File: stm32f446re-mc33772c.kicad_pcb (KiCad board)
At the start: 2 copper layers, 116 parts, among them J1 Conn_01x02, J2 USB_B_Micro, J3 Conn_01x03, J4 Conn_01x06, J5 S7B-XH-A, J6 SM06B-GHS-TB, U1 STM32F446RETx, U2 MC33772CTP1AE, U3 LD1086D2M33TR, U4 AMS1117-3.3, U6 LMR51450SDRRR, U7 SN65HVD232, Y1 16MHz

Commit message: good placement
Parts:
- C10, C11, C18, C19, C48, C49, C50, C51, C52, C53, C54, C58, C59, C6, C60, C7, C8, C9, R24, R25, R26, R27, R28, R29, R30, R31, R32, R35, R36, R37: moved to B.Cu
- J3: footprint Connector_PinHeader_2.54mm:PinHeader_1x03_P2.54mm_Vertical -> Connector_PinHeader_1.00mm:PinHeader_1x03_P1.00mm_Vertical
- J4: value Conn_01x06 -> Conn_01x03; footprint Connector_PinHeader_2.54mm:PinHeader_1x06_P2.54mm_Vertical -> Connector_PinHeader_1.00mm:PinHeader_1x03_P1.00mm_Vertical
- moved C26 109.7 mm to (178.0, 54.0), turned to -90 degrees
- moved R7 106.9 mm to (176.4, 52.6), turned to 90 degrees
- moved R36 106.6 mm to (191.5, 49.0), turned to 0 degrees
- moved J3 104.8 mm to (218.9, 94.2), turned to 0 degrees
- moved D3 104.6 mm to (174.4, 53.2), turned to -90 degrees
- moved C59 104.3 mm to (191.5, 52.0), turned to 180 degrees
- moved C61 103.4 mm to (185.5, 44.0)
- moved U6 103.1 mm to (182.5, 44.0)
- moved C57 102.6 mm to (175.6, 46.7), turned to 180 degrees
- moved C56 101.6 mm to (175.6, 44.4), turned to 180 degrees
- moved C55 101.5 mm to (176.1, 42.4), turned to 180 degrees
- moved D1 100.3 mm to (159.0, 44.5)
- moved R37 99.4 mm to (192.4, 55.5), turned to 90 degrees
- moved R35 98.5 mm to (191.0, 55.5), turned to 90 degrees
- moved D2 98.1 mm to (165.6, 46.0)
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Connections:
- J3 pad 1: BAT_3.3V -> BP-C1M
- J3 pad 2: LDO_3.3V -> SWDIO
- J3 pad 3: USB_3.3V -> SWCLK
- J4 pad 1: LDO_3.3V -> BAT_3.3V
- J4 pad 2: BP-C1M -> LDO_3.3V
- J4 pad 3: SWDIO -> USB_3.3V
- U1 pad 55: SWO -> unconnected-(U1-PB3-Pad55)
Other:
- board outline added: 99 x 62.5 mm
- board text removed: "BOOT0"
- board text removed: "SWD"

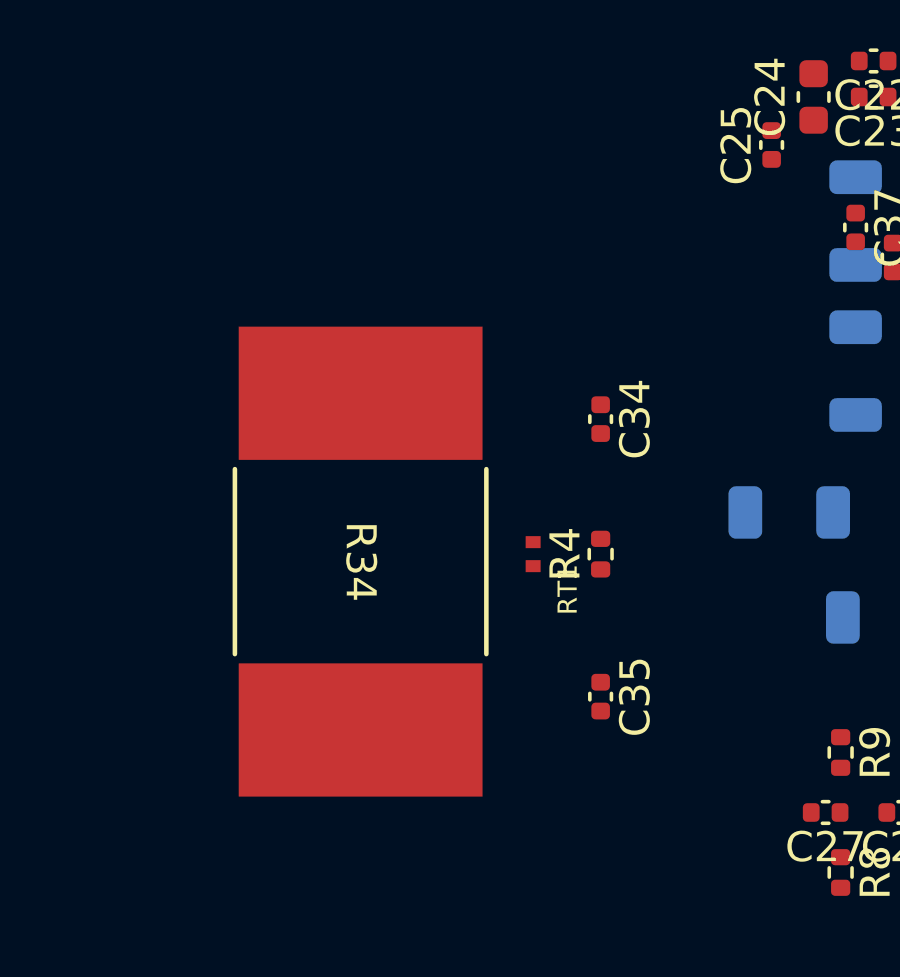
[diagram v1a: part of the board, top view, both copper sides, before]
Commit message: GND the whole in2.Cu
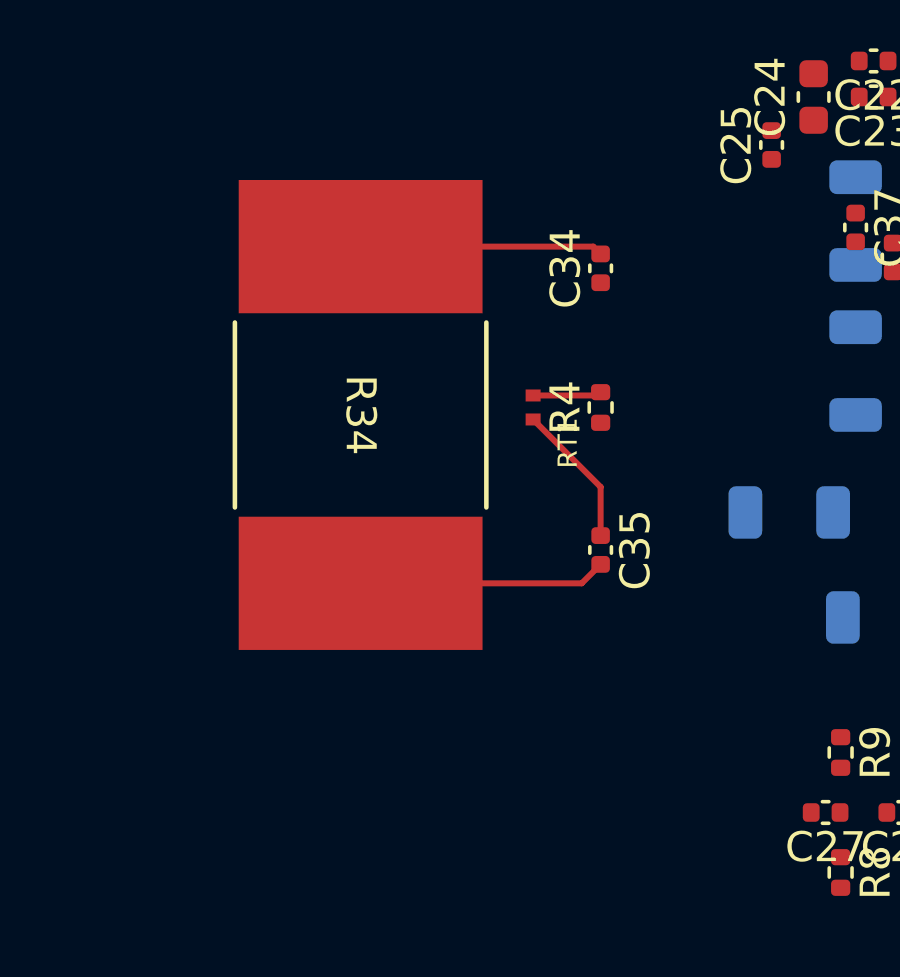
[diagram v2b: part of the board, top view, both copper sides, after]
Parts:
- moved C34 5.03 mm to (145.5, 66.1), turned to 90 degrees
- moved C35 4.89 mm to (145.5, 75.5)
- moved R34 4.89 mm to (137.5, 71.0)
- moved R4 4.89 mm to (145.5, 70.8)
- moved RT1 4.89 mm to (143.2, 70.8)
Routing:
- net BP-C1M: track 0.00 -> 12.9 mm
- net Pack-: track 0.00 -> 8.26 mm
- net Net-(R33-Pad2): track 0.00 -> 2.30 mm
- added copper zone on In2.Cu, net GND
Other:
- copper layers 2 -> 4
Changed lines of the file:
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@@
 	(layers
 		(0 "F.Cu" mixed)
+		(4 "In1.Cu" signal)
+		(6 "In2.Cu" signal)
 		(2 "B.Cu" signal)
 		(9 "F.Adhes" user "F.Adhesive")
@@
 	)
 	(setup
+		(stackup
+			(layer "F.SilkS"
+				(type "Top Silk Screen")
+			)
+			(layer "F.Paste"
+				(type "Top Solder Paste")
+			)
+			(layer "F.Mask"
+				(type "Top Solder Mask")
+				(thickness 0.01)
+			)
+			(layer "F.Cu"
+				(type "copper")
+				(thickness 0.035)
+			)
+			(layer "dielectric 1"
+				(type "prepreg")
+				(thickness 0.1)
+				(material "FR4")
+				(epsilon_r 4.5)
+				(loss_tangent 0.02)
+			)
+			(layer "In1.Cu"
+				(type "copper")
+				(thickness 0.035)
+			)
+			(layer "dielectric 2"
+				(type "core")
+				(thickness 1.24)
+				(material "FR4")
+				(epsilon_r 4.5)
+				(loss_tangent 0.02)
+			)
+			(layer "In2.Cu"
+				(type "copper")
+				(thickness 0.035)
+			)
+			(layer "dielectric 3"
+				(type "prepreg")
+				(thickness 0.1)
+				(material "FR4")
+				(epsilon_r 4.5)
+				(loss_tangent 0.02)
+			)
+			(layer "B.Cu"
+				(type "copper")
+				(thickness 0.035)
+			)
+			(layer "B.Mask"
+				(type "Bottom Solder Mask")
+				(thickness 0.01)
+			)
+			(layer "B.Paste"
+				(type "Bottom Solder Paste")
+			)
+			(layer "B.SilkS"
+				(type "Bottom Silk Screen")
+			)
+			(copper_finish "None")
+			(dielectric_constraints no)
+		)
 		(pad_to_mask_clearance 0)
 		(allow_soldermask_bridges_in_footprints no)
@@
 		(capping no)
 		(filling no)
+		(zone_defaults)
 		(pcbplotparams
 			(layerselection 0x00000000_00000000_55555555_5755f5ff)
@@
 	(footprint "Resistor_SMD:R_0402_1005Metric"
 		(layer "F.Cu")
-		(at 145.5 75.6382 90)
+		(at 145.5 70.75 90)
 		(descr "Resistor SMD 0402 (1005 Metric), square (rectangular) end terminal, IPC-7351 nominal, (Body size source: IPC-SM-782 page 72, https://www.pcb-3d.com/wordpress/wp-content/uploads/ipc-sm-782a_amendment_1_and_2.pdf)")
 		(tags "resistor")
@@
 	(footprint "Capacitor_SMD:C_0402_1005Metric"
 		(layer "F.Cu")
-		(at 145.5 71.1382 -90)
+		(at 145.5 66.1118 90)
 		(descr "Capacitor SMD 0402 (1005 Metric), square (rectangular) end terminal, IPC-7351 nominal, (Body size source: IPC-SM-782 page 76, https://www.pcb-3d.com/wordpress/wp-content/uploads/ipc-sm-782a_amendment_1_and_2.pdf)")
 		(tags "capacitor")
@@
 		(duplicate_pad_numbers_are_jumpers no)
 		(fp_line
-			(start -0.107836 0.36)
-			(end 0.107836 0.36)
+			(start -0.107836 -0.36)
+			(end 0.107836 -0.36)
 			(stroke
 				(width 0.12)
@@
 		)
 		(fp_line
-			(start -0.107836 -0.36)
-			(end 0.107836 -0.36)
+			(start -0.107836 0.36)
+			(end 0.107836 0.36)
 			(stroke
 				(width 0.12)
@@
 		)
 		(pad "1" smd roundrect
-			(at -0.48 0 270)
+			(at -0.48 0 90)
 			(size 0.56 0.62)
 			(layers "F.Cu" "F.Mask" "F.Paste")
@@
 		)
 		(pad "2" smd roundrect
-			(at 0.48 0 270)
+			(at 0.48 0 90)
 			(size 0.56 0.62)
 			(layers "F.Cu" "F.Mask" "F.Paste")
@@
 	(footprint "MyFootLib:WSLP5931L1000FEA"
 		(layer "F.Cu")
-		(at 137.5 75.8882 -90)
+		(at 137.5 71 -90)
 		(tags "WSLP5931L1000FEA ")
 		(property "Reference" "R34"
@@
 			(polygon
 				(pts
-					(xy 141.5132 72.548099) (xy 141.5132 79.228301) (xy 133.4868 79.228301) (xy 133.4868 72.548099)
+					(xy 141.5132 67.659899) (xy 141.5132 74.340101) (xy 133.4868 74.340101) (xy 133.4868 67.659899)
 				)
 			)
@@
 	(footprint "Capacitor_SMD:C_0402_1005Metric"
 		(layer "F.Cu")
-		(at 145.5 80.3882 -90)
+		(at 145.5 75.5 -90)
 		(descr "Capacitor SMD 0402 (1005 Metric), square (rectangular) end terminal, IPC-7351 nominal, (Body size source: IPC-SM-782 page 76, https://www.pcb-3d.com/wordpress/wp-content/uploads/ipc-sm-782a_amendment_1_and_2.pdf)")
 		(tags "capacitor")
@@
 	(footprint "MyFootLib:THERM_NTCG104BH103HT1"
 		(layer "F.Cu")
-		(at 143.25 75.6382 -90)
+		(at 143.25 70.75 -90)
 		(property "Reference" "RT1"
 			(at 1.182 -1.1564 90)
@@
 		(layer "Edge.Cuts")
 	)
-	(gr_text_box "PACK+"
-		(start 123.625 102.313)
-		(end 133.375 97.5)
+	(gr_text_box "GND"
+		(start 179 94.0935)
+		(end 185.5 98.9065)
 		(margins 1.0025 1.0025 1.0025 1.0025)
 		(layer "F.Cu")
@@
 		(knockout no)
 	)
-	(gr_text_box "BAT+"
-		(start 124 53)
-		(end 132.5 48.187)
-		(margins 1.0025 1.0025 1.0025 1.0025)
+	(segment
+		(start 145.5 73.4)
+		(end 143.25 71.15)
+		(width 0.2)
 		(layer "F.Cu")
-		(effects
-			(font
-				(size 1.5 1.5)
-				(thickness 0.3)
-				(bold yes)
-			)
-			(justify left top)
-		)
-		(border yes)
-		(stroke
-			(width 0.2)
-			(type solid)
-		)
-		(knockout no)
+		(net "BP-C1M")
 	)
-	(gr_text_box "PACK-"
-		(start 132.5 94.2012)
-		(end 142.25 89.3882)
-		(margins 1.0025 1.0025 1.0025 1.0025)
+	(segment
+		(start 145.5 75.02)
+		(end 145.5 73.4)
+		(width 0.2)
 		(layer "F.Cu")
-		(effects
-			(font
-				(size 1.5 1.5)
-				(thickness 0.3)
-				(bold yes)
-			)
-			(justify left top)
-		)
-		(border yes)
-		(stroke
-			(width 0.2)
-			(type solid)
-		)
-		(knockout no)
+		(net "BP-C1M")
 	)
-	(gr_text_box "BAT-"
-		(start 133.75 63.5447)
-		(end 141.25 58.7317)
-		(margins 1.0025 1.0025 1.0025 1.0025)
+	(segment
+		(start 145.2564 65.3882)
+		(end 145.5 65.6318)
+		(width 0.2)
 		(layer "F.Cu")
-		(effects
-			(font
-				(size 1.5 1.5)
-				(thickness 0.3)
-				(bold yes)
-			)
-			(justify left top)
-		)
-		(border yes)
-		(stroke
-			(width 0.2)
-			(type solid)
-		)
-		(knockout no)
+		(net "BP-C1M")
 	)
-	(gr_text_box "GND"
-		(start 179 94.0935)
-		(end 185.5 98.9065)
-		(margins 1.0025 1.0025 1.0025 1.0025)
+	(segment
+		(start 137.5 65.3882)
+		(end 145.2564 65.3882)
+		(width 0.2)
 		(layer "F.Cu")
-		(effects
-			(font
-				(size 1.5 1.5)
-				(thickness 0.3)
-				(bold yes)
-			)
-			(justify left top)
+		(net "BP-C1M")
+	)
+	(segment
+		(start 145.39 70.35)
+		(end 145.5 70.24)
+		(width 0.2)
+		(layer "F.Cu")
+		(net "Net-(R33-Pad2)")
+	)
+	(segment
+		(start 143.25 70.35)
+		(end 145.39 70.35)
+		(width 0.2)
+		(layer "F.Cu")
+		(net "Net-(R33-Pad2)")
+	)
+	(segment
+		(start 137.5 76.6118)
+		(end 144.8682 76.6118)
+		(width 0.2)
+		(layer "F.Cu")
+		(net "Pack-")
+	)
+	(segment
+		(start 144.8682 76.6118)
+		(end 145.5 75.98)
+		(width 0.2)
+		(layer "F.Cu")
+		(net "Pack-")
+	)
+	(zone
+		(net "GND")
+		(layer "In2.Cu")
+		(hatch edge 0.5)
+		(connect_pads
+			(clearance 0.5)
 		)
-		(border yes)
-		(stroke
-			(width 0.2)
-			(type solid)
+		(min_thickness 0.25)
+		(fill yes
+			(thermal_gap 0.5)
+			(thermal_bridge_width 0.5)
+			(island_removal_mode 0)
+		)
+		(polygon
+			(pts
+				(xy 121.5 40.5) (xy 121.5 103) (xy 220.5 103) (xy 220.5 40.5)
+			)
 		)
-		(knockout no)
 	)
 	(embedded_fonts no)

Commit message: start routing
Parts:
- turned R20 to -90 degrees
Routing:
- net Pack_24V: track 0.00 -> 75.5 mm
- net BP-C1M: track 12.9 -> 69.8 mm, vias 0 -> 19
- net Pack-: track 8.26 -> 24.1 mm
- net BP-C5P: track 0.00 -> 8.03 mm, vias 0 -> 1
- net BP-C2P: track 0.00 -> 7.92 mm, vias 0 -> 1
- net BP-C6P: track 0.00 -> 7.91 mm, vias 0 -> 1
- net BP-C4P: track 0.00 -> 7.91 mm, vias 0 -> 1
- net BP-C3P: track 0.00 -> 7.81 mm, vias 0 -> 1
- net BP-C1P: track 0.00 -> 7.80 mm, vias 0 -> 1
- net Net-(C33-Pad1): track 0.00 -> 2.98 mm
- net Net-(C32-Pad1): track 0.00 -> 2.98 mm
- net Net-(C31-Pad1): track 0.00 -> 2.98 mm
- net Net-(C30-Pad1): track 0.00 -> 2.98 mm
- net Net-(C29-Pad1): track 0.00 -> 2.98 mm
- net Net-(C28-Pad1): track 0.00 -> 2.98 mm
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- added copper zone on F.Cu, net BP-C1M
- added copper zone on F.Cu, net Pack-
- added copper zone on F.Cu, net Pack_24V
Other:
- board size 99 x 62.5 mm -> 105.7 x 62.5 mm
- board text added: "B+"
- board text added: "B-"
- board text added: "P+"
- board text added: "P-"

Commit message: freerouting weird wiring
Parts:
- moved D4 2.70 mm to (178.2, 96.0)
- moved C64 2.08 mm to (213.6, 86.6)
- moved C63 2.08 mm to (212.2, 86.4)
- moved C4 1.83 mm to (199.2, 50.4), turned to 90 degrees
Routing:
- net BP-C1M: track 69.8 -> 243.5 mm, vias 19 -> 49
- net LDO_3.3V: track 0.00 -> 144.7 mm, vias 0 -> 2
- net Buck_5V: track 0.00 -> 71.9 mm, vias 0 -> 2
- net BP-C6P: track 7.91 -> 79.5 mm, vias 1 -> 2
- net Pack-: track 24.1 -> 73.1 mm, vias 0 -> 2
- net D+: track 0.00 -> 46.8 mm, vias 0 -> 2
- net D-: track 0.00 -> 41.3 mm, vias 0 -> 2
- net VBAT_PROT_24V: track 0.00 -> 35.6 mm
- net SWDIO: track 0.00 -> 35.5 mm, vias 0 -> 1
- net AFE_VCOM: track 0.00 -> 34.7 mm, vias 0 -> 2
- net SPI1_SCK: track 0.00 -> 33.1 mm, vias 0 -> 2
- net SWCLK: track 0.00 -> 31.7 mm
- net SPI1_MOSI: track 0.00 -> 31.1 mm, vias 0 -> 2
- net SPI1_NSS: track 0.00 -> 30.4 mm, vias 0 -> 2
- net Net-(J1-Pin_2): track 0.00 -> 28.0 mm
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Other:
- board text added: "BOOT0"

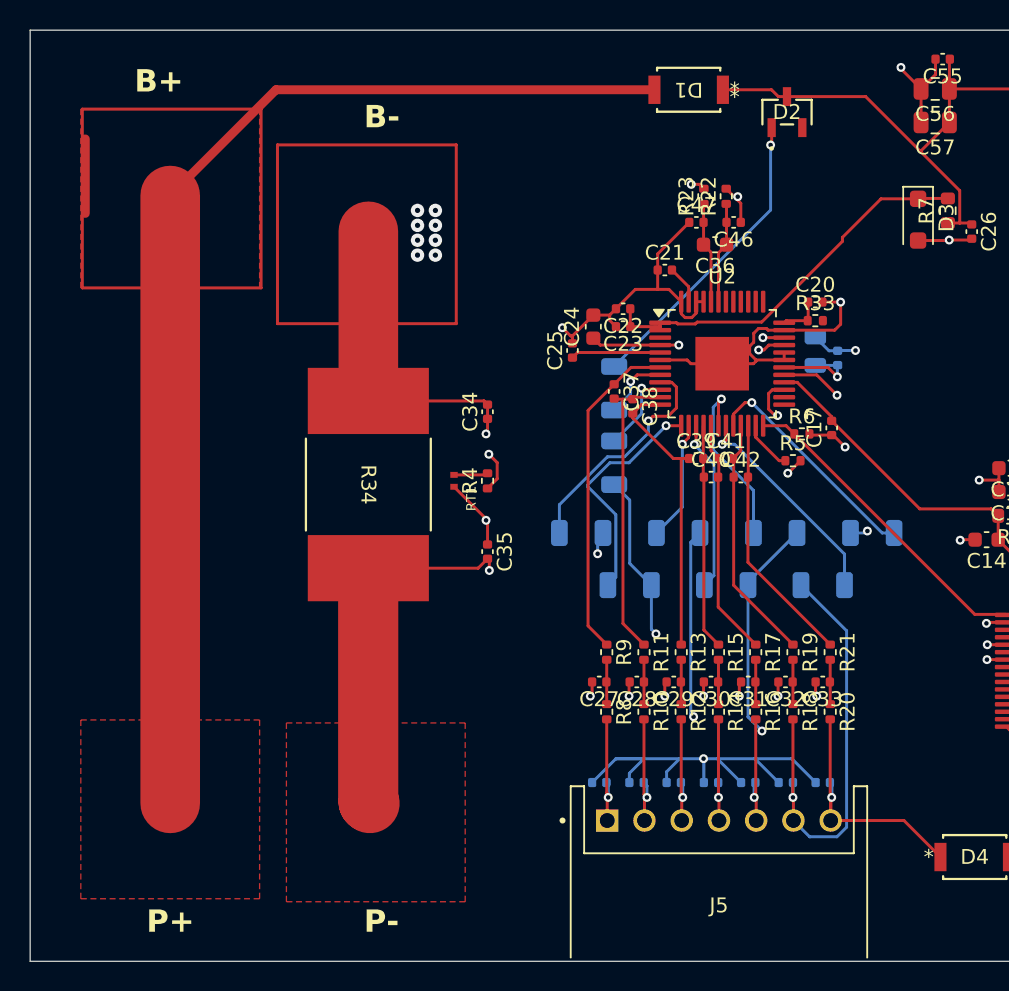
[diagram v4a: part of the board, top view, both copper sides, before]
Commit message: add pad for B and P
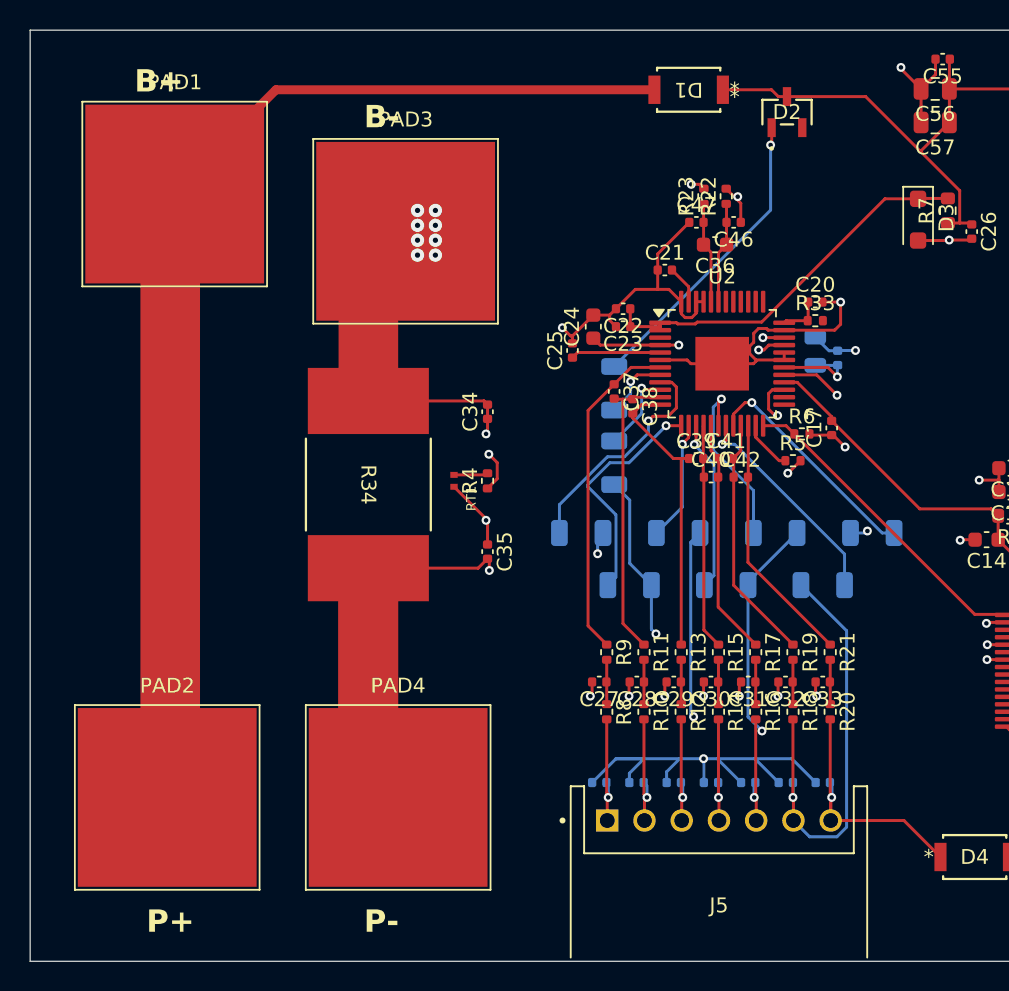
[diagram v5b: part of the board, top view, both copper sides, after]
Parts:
- added PAD1: pad, MyFootLib:INPUT_PAD, F.Cu at (124.5, 51.5)
- added PAD2: pad, MyFootLib:INPUT_PAD, F.Cu at (124.0, 92.0)
- added PAD3: pad, MyFootLib:INPUT_PAD, F.Cu at (140.0, 54.0)
- added PAD4: pad, MyFootLib:INPUT_PAD, F.Cu at (139.5, 92.0)
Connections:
- C10 pad 2: BP-C1M -> Rsense_P
- C11 pad 2: BP-C1M -> Rsense_P
- C12 pad 2: BP-C1M -> Rsense_P
- C13 pad 2: BP-C1M -> Rsense_P
- C14 pad 2: BP-C1M -> Rsense_P
- C15 pad 2: BP-C1M -> Rsense_P
- C16 pad 2: BP-C1M -> Rsense_P
- C17 pad 1: BP-C1M -> Rsense_P
- C18 pad 1: BP-C1M -> Rsense_P
- C19 pad 1: BP-C1M -> Rsense_P
- C2 pad 2: BP-C1M -> Rsense_P
- C20 pad 2: BP-C1M -> Rsense_P
- C21 pad 1: BP-C1M -> Rsense_P
- C22 pad 2: BP-C1M -> Rsense_P
- C23 pad 2: BP-C1M -> Rsense_P
- C24 pad 2: BP-C1M -> Rsense_P
- C25 pad 2: BP-C1M -> Rsense_P
- C26 pad 2: BP-C1M -> Rsense_P
- C27 pad 2: BP-C1M -> Rsense_P
- C28 pad 2: BP-C1M -> Rsense_P
- C29 pad 2: BP-C1M -> Rsense_P
- C3 pad 2: BP-C1M -> Rsense_P
- C30 pad 2: BP-C1M -> Rsense_P
- C31 pad 2: BP-C1M -> Rsense_P
- C32 pad 2: BP-C1M -> Rsense_P
- C33 pad 2: BP-C1M -> Rsense_P
- C34 pad 1: BP-C1M -> Rsense_P
- C34 pad 2: BP-C1M -> Rsense_P
- C35 pad 1: BP-C1M -> Rsense_P
- C4 pad 2: BP-C1M -> Rsense_P
- C46 pad 1: BP-C1M -> Rsense_P
- C47 pad 1: BP-C1M -> Rsense_P
- C48 pad 2: BP-C1M -> Rsense_P
- C49 pad 2: BP-C1M -> Rsense_P
- C5 pad 2: BP-C1M -> Rsense_P
- C50 pad 2: BP-C1M -> Rsense_P
- C51 pad 2: BP-C1M -> Rsense_P
- C52 pad 2: BP-C1M -> Rsense_P
- C53 pad 2: BP-C1M -> Rsense_P
- C54 pad 2: BP-C1M -> Rsense_P
- C55 pad 2: BP-C1M -> Rsense_P
- C56 pad 2: BP-C1M -> Rsense_P
- C57 pad 2: BP-C1M -> Rsense_P
- C58 pad 1: BP-C1M -> Rsense_P
- C6 pad 2: BP-C1M -> Rsense_P
- C60 pad 2: BP-C1M -> Rsense_P
- C63 pad 2: BP-C1M -> Rsense_P
- C64 pad 2: BP-C1M -> Rsense_P
- C7 pad 2: BP-C1M -> Rsense_P
- C8 pad 2: BP-C1M -> Rsense_P
- C9 pad 2: BP-C1M -> Rsense_P
- D3 pad 2: BP-C1M -> Rsense_P
- D4 pad 2: BP-C1M -> Rsense_P
- J2 pad 5: BP-C1M -> Rsense_P
- J2 pad SH: BP-C1M -> Rsense_P
- J3 pad 1: BP-C1M -> Rsense_P
- J6 pad 5: BP-C1M -> Rsense_P
- J6 pad 6: BP-C1M -> Rsense_P
- R1 pad 2: BP-C1M -> Rsense_P
- R22 pad 2: BP-C1M -> Rsense_P
- R34 pad 1: BP-C1M -> Rsense_P
- R36 pad 2: BP-C1M -> Rsense_P
- R6 pad 2: BP-C1M -> Rsense_P
- RT1 pad 2: BP-C1M -> Rsense_P
- U1 pad 12: BP-C1M -> Rsense_P
- U1 pad 18: BP-C1M -> Rsense_P
- U1 pad 31: BP-C1M -> Rsense_P
- U1 pad 47: BP-C1M -> Rsense_P
- U1 pad 63: BP-C1M -> Rsense_P
- U2 pad 31: BP-C1M -> Rsense_P
- U2 pad 32: BP-C1M -> Rsense_P
- U2 pad 35: BP-C1M -> Rsense_P
- U2 pad 45: BP-C1M -> Rsense_P
- U2 pad 46: BP-C1M -> Rsense_P
- U2 pad 48: BP-C1M -> Rsense_P
- U2 pad 49: BP-C1M -> Rsense_P
- U2 pad 6: BP-C1M -> Rsense_P
- U3 pad 1: BP-C1M -> Rsense_P
- U4 pad 1: BP-C1M -> Rsense_P
- U6 pad 13: BP-C1M -> Rsense_P
- U6 pad 5: BP-C1M -> Rsense_P
- U6 pad 6: BP-C1M -> Rsense_P
- U6 pad 8: BP-C1M -> Rsense_P
- U7 pad 2: BP-C1M -> Rsense_P
- Y1 pad 2: BP-C1M -> Rsense_P
- Y1 pad 4: BP-C1M -> Rsense_P
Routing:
- net BP-C1M: track 243.5 -> 48.4 mm, vias 49 -> 5
- net Rsense_P: track 0.00 -> 195.1 mm, vias 0 -> 44
- net Pack_24V: track 81.2 -> 76.2 mm
- added copper zone on In2.Cu, net Rsense_P
- removed copper zone on F.Cu, net BP-C1M
- removed copper zone on In2.Cu, net GND
- removed copper zone on F.Cu, net Pack-
- removed copper zone on F.Cu, net Pack_24V
